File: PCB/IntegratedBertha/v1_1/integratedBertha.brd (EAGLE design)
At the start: 108.1 x 84.6 mm, 100 parts, among them CON1 SPI, IC1 REG1117, IC2 AD8223, J7 22--02, Q1 BSP75, Q2 BSP75, Q4 BSP75, Q5 BSP75, Q6 BSP75, Q7 IRF3704S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

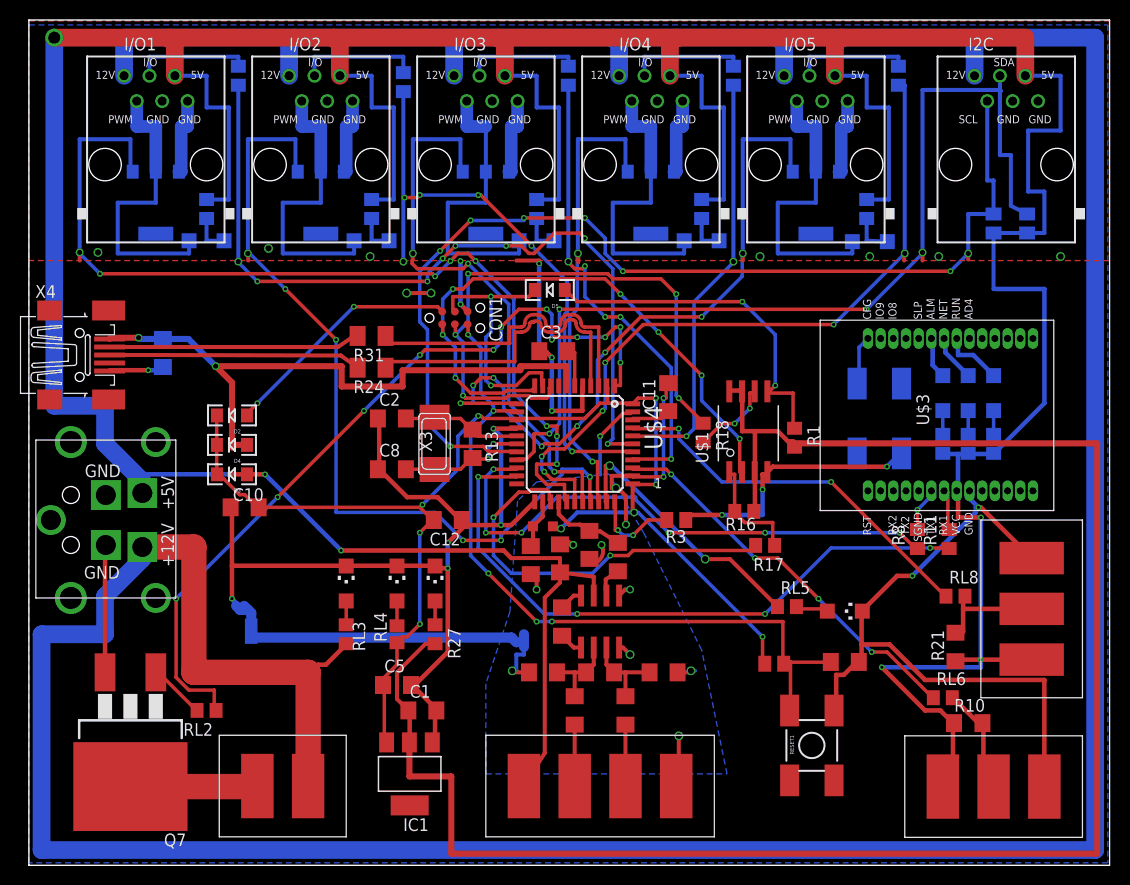
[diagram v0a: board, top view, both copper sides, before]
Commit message: adapted label positions in integrated bertha 1.1 and created new gerbers
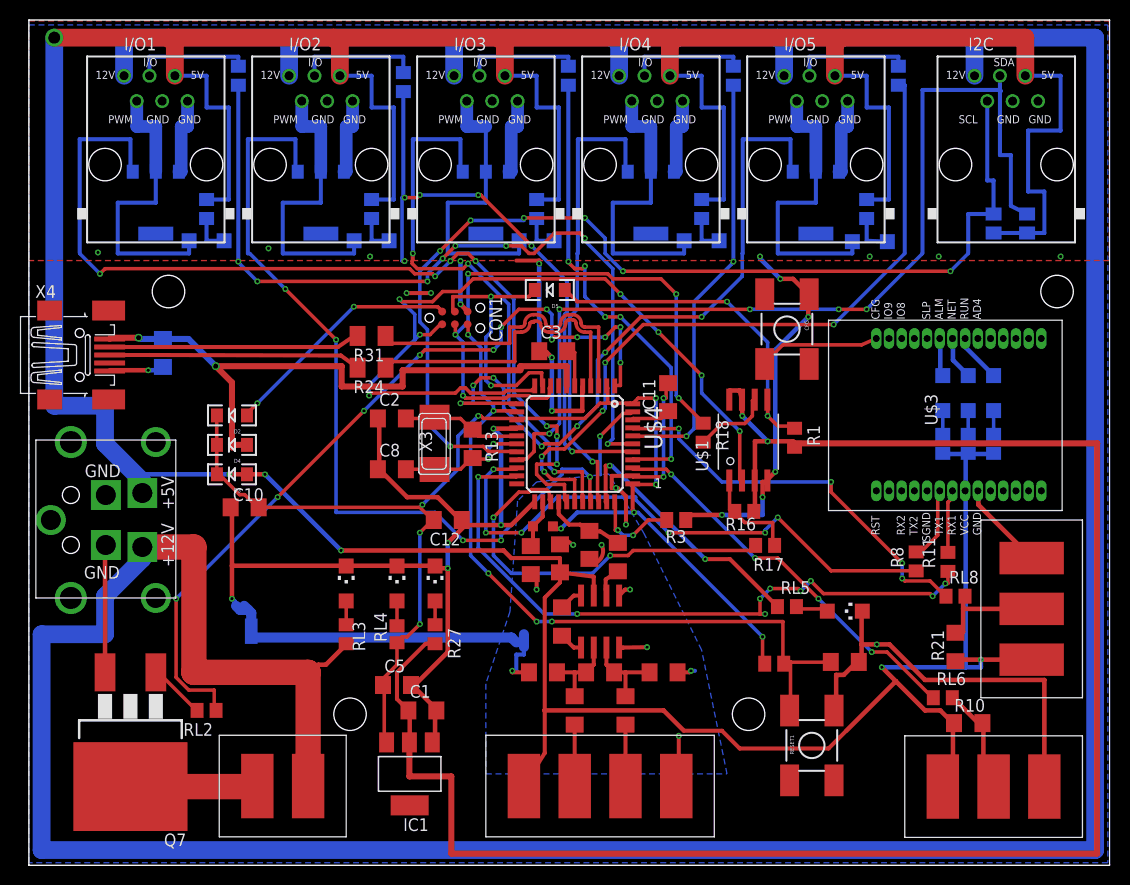
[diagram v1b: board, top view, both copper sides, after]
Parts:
- moved CFG 12.9 mm to (75.8, 50.9), flipped to the top, turned to 270 degrees
- moved R11 2.29 mm to (91.9, 27.6)
- moved R8 2.24 mm to (88.8, 27.6)
- moved U$1 0.84 mm to (72.0, 38.6)
- moved U$3 0.84 mm to (92.4, 42.9)
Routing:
- net MISO: track 60.6 -> 80.5 mm
- net +5V: track 470.7 -> 479.6 mm, vias 7 -> 6
- net N$35: track 5.01 -> 12.1 mm
- net GND: track 284.9 -> 280.4 mm, vias 25 -> 26
- net N$24: track 4.45 -> 7.50 mm, vias 1 -> 0
- net TX: track 63.6 -> 66.1 mm, vias 4 -> 9
- net RX: track 56.1 -> 58.2 mm
- net N$11: track 4.22 -> 6.38 mm
- net A5: track 38.9 -> 40.4 mm, vias 2 -> 4
- net AGND: track 78.0 -> 79.4 mm
- net GND1: track 6.13 -> 4.88 mm
- net D5*: track 47.3 -> 46.4 mm, vias 2 -> 1
- net N$10: track 11.2 -> 10.4 mm
- net SDA: track 98.0 -> 97.2 mm, vias 4 -> 5
- net D8*: track 72.9 -> 72.1 mm, vias 6 -> 5
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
